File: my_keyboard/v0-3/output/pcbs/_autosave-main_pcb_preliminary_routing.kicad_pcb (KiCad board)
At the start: 2 copper layers, 136.8 x 106.8 mm, 27 parts

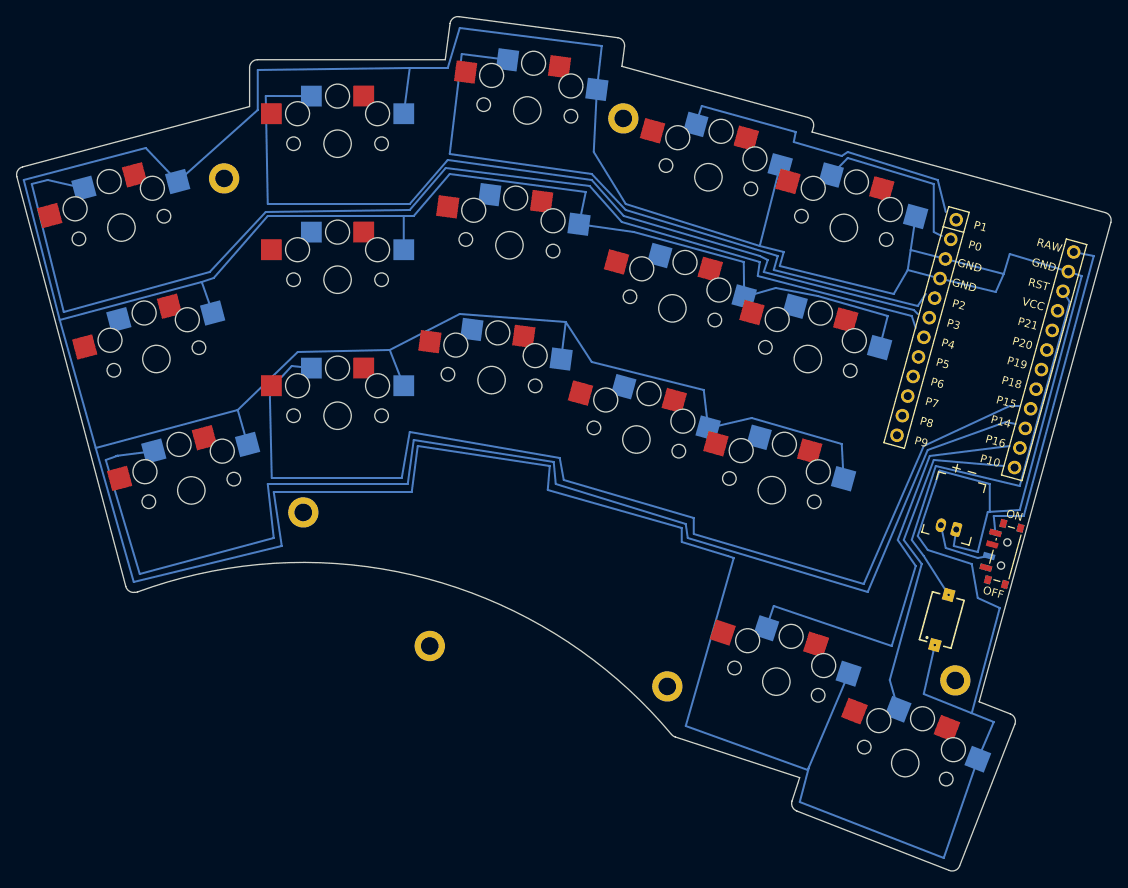
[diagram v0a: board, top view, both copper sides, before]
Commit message: Add docs and v0-3
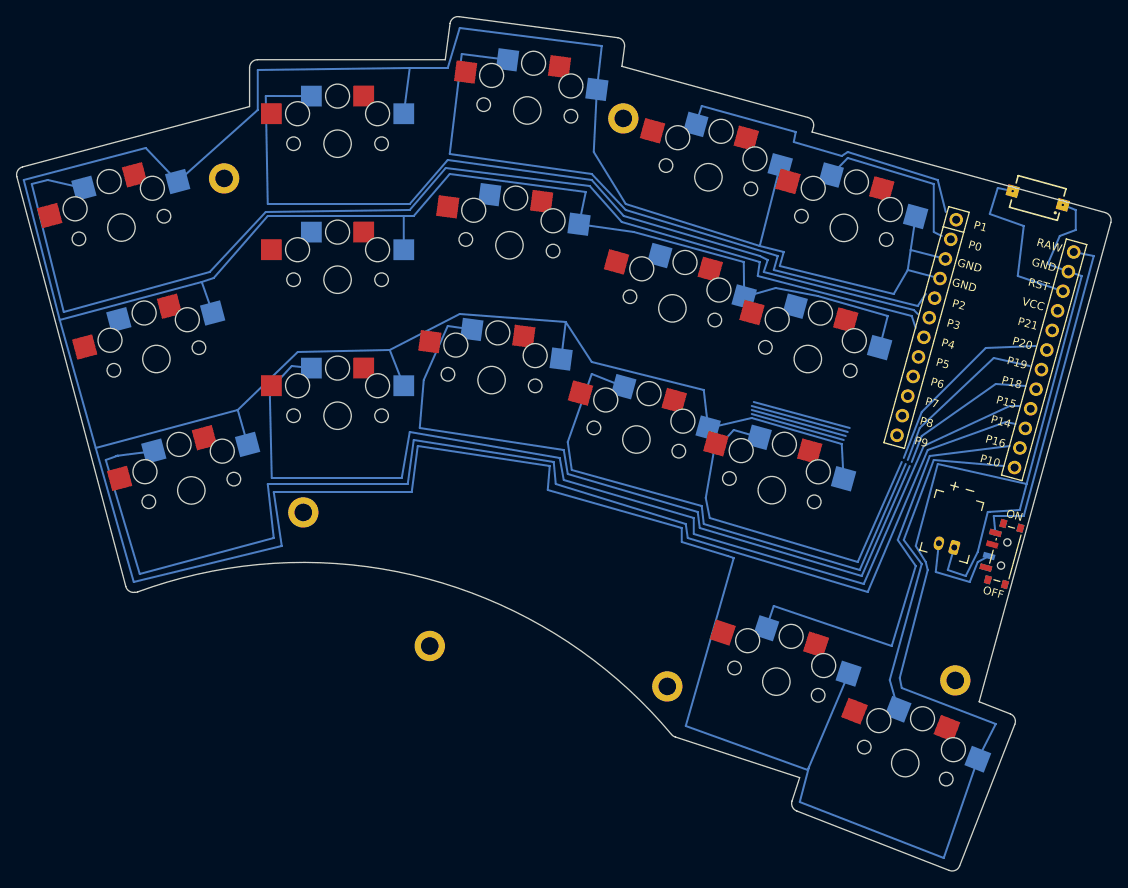
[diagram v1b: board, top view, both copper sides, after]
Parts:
- moved S18 54.1 mm to (187.0, 45.2), turned to 164.64 degrees
- moved JST1 2.26 mm to (175.6, 88.7)
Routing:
- net (no net): track 0.00 -> 112.9 mm
- net P15: track 0.00 -> 92.8 mm
- net P16: track 0.00 -> 70.7 mm
- net P18: track 0.00 -> 48.4 mm
- net RST: track 54.2 -> 22.1 mm
- net GND: track 813.9 -> 792.9 mm
- net PWR_SW: track 8.53 -> 12.3 mm
